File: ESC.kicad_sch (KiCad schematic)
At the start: 37 parts, among them Q1 SP40N03GNJ, Q11 SP40N03GNJ, Q3 SP40N03GNJ, Q5 SP40N03GNJ, Q7 SP40N03GNJ, Q9 SP40N03GNJ, U1 AT32F421G8U7, U3 NSG2065Q_C53463328

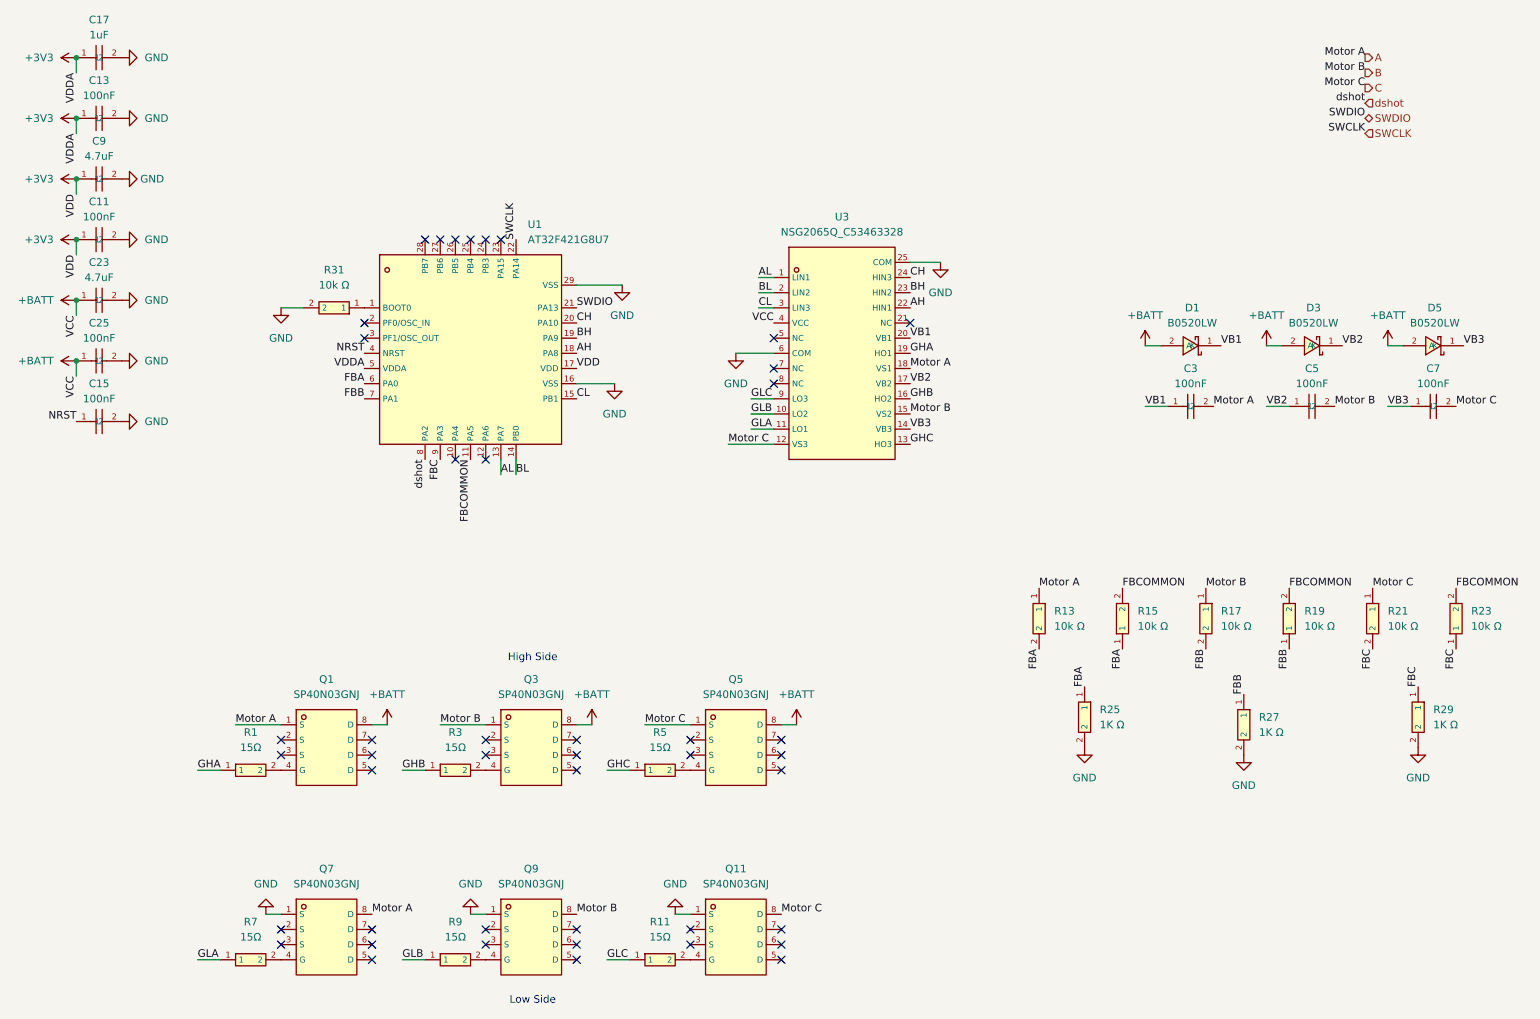
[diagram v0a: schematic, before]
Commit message: Bridges Placed
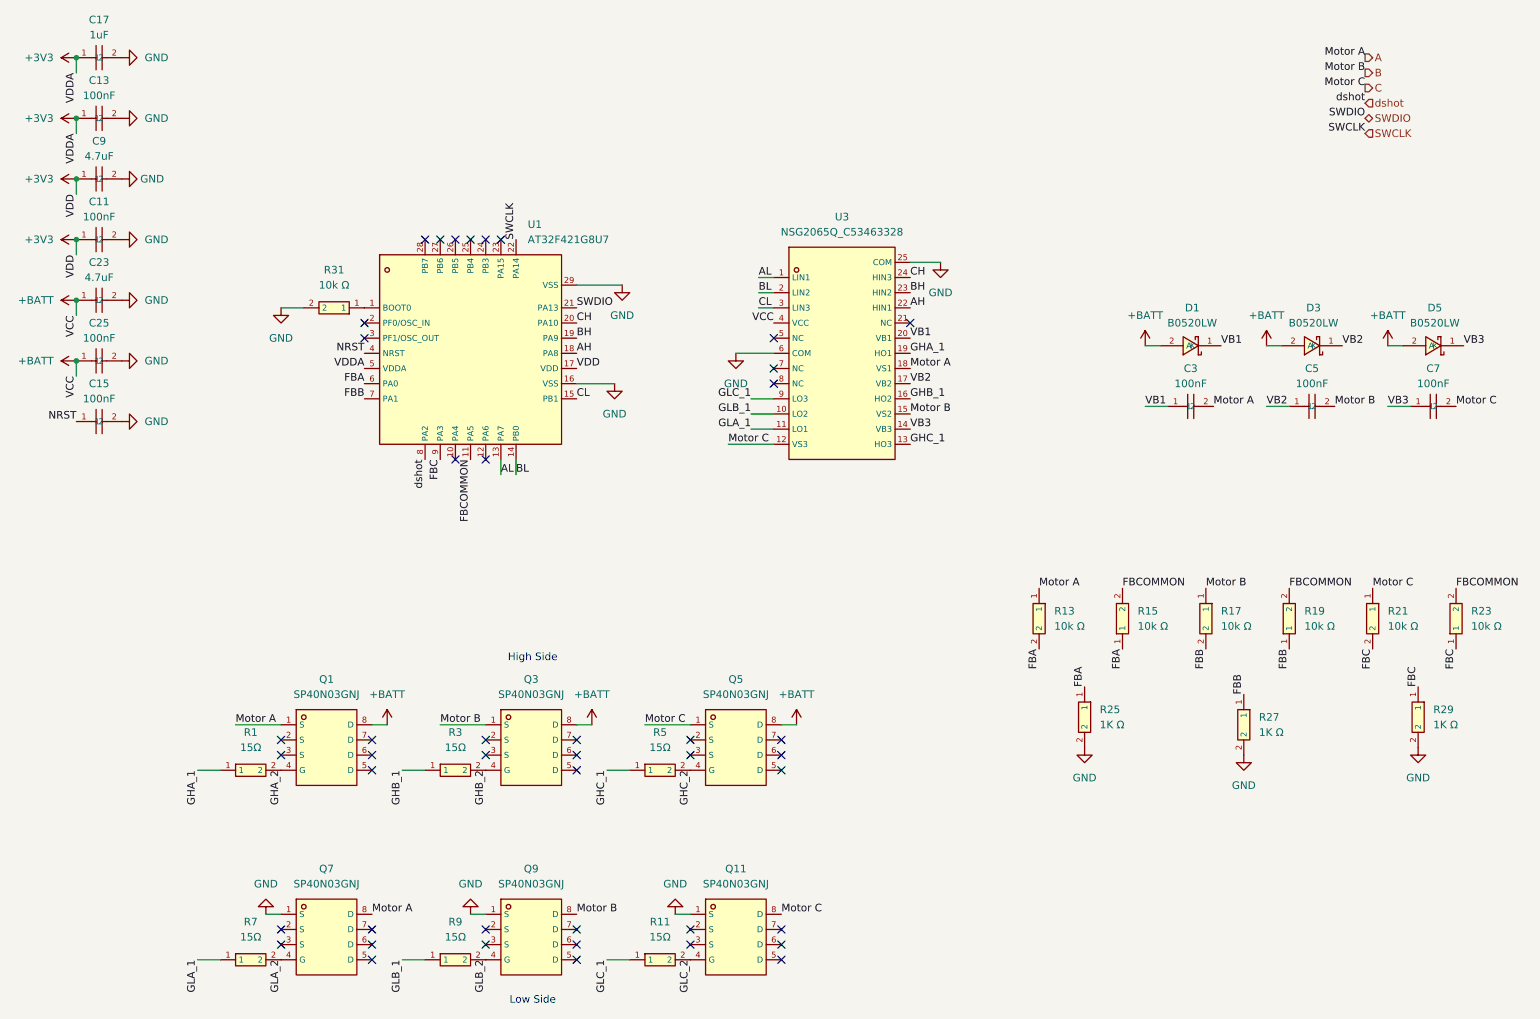
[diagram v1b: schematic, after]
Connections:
- net GHB_2: now reaches Q3.4 (G), R3.2
- net GHA_2: now reaches Q1.4 (G), R1.2
- net GLA_2: now reaches Q7.4 (G), R7.2
- net GLC_2: now reaches Q11.4 (G), R11.2
- net GLB_2: now reaches Q9.4 (G), R9.2
- net GHC_2: now reaches Q5.4 (G), R5.2
- net GHA renamed GHA_1
- net GHB renamed GHB_1
- net GHC renamed GHC_1
- net GLA renamed GLA_1
- net GLB renamed GLB_1
- net GLC renamed GLC_1
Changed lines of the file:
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@@
 		)
 	)
-	(label "GHA"
+	(label "GHA_1"
 		(at 165.1 72.39 0)
 		(effects
@@
 		)
 	)
-	(label "GLB"
-		(at 80.01 173.99 0)
+	(label "GLB_1"
+		(at 80.01 173.99 270)
 		(effects
 			(font
 				(size 1.27 1.27)
 			)
-			(justify left bottom)
+			(justify right bottom)
 		)
 	)
-	(label "GLC"
-		(at 114.3 173.99 0)
+	(label "GLC_1"
+		(at 114.3 173.99 270)
 		(effects
 			(font
 				(size 1.27 1.27)
 			)
-			(justify left bottom)
+			(justify right bottom)
 		)
 	)
@@
 		)
 	)
+	(label "GHC_2"
+		(at 128.27 142.24 270)
+		(effects
+			(font
+				(size 1.27 1.27)
+			)
+			(justify right bottom)
+		)
+	)
 	(label "FBA"
 		(at 194.31 128.27 90)
@@
 		)
 	)
+	(label "GLA_2"
+		(at 59.69 173.99 270)
+		(effects
+			(font
+				(size 1.27 1.27)
+			)
+			(justify right bottom)
+		)
+	)
 	(label "AH"
 		(at 165.1 64.77 0)
@@
 		)
 	)
-	(label "GHC"
-		(at 114.3 142.24 0)
+	(label "GHC_1"
+		(at 114.3 142.24 270)
 		(effects
 			(font
 				(size 1.27 1.27)
 			)
-			(justify left bottom)
+			(justify right bottom)
 		)
 	)
@@
 		)
 	)
-	(label "GLC"
-		(at 138.43 80.01 0)
+	(label "GLC_1"
+		(at 138.43 80.01 180)
 		(effects
 			(font
 				(size 1.27 1.27)
 			)
-			(justify left bottom)
+			(justify right bottom)
 		)
 	)
@@
 		)
 	)
+	(label "GHA_2"
+		(at 59.69 142.24 270)
+		(effects
+			(font
+				(size 1.27 1.27)
+			)
+			(justify right bottom)
+		)
+	)
 	(label "AL"
 		(at 139.7 59.69 0)
@@
 		)
 	)
+	(label "GLC_2"
+		(at 128.27 173.99 270)
+		(effects
+			(font
+				(size 1.27 1.27)
+			)
+			(justify right bottom)
+		)
+	)
 	(label "VB2"
 		(at 237.49 71.12 0)
@@
 		)
 	)
-	(label "GLA"
-		(at 138.43 85.09 0)
+	(label "GLA_1"
+		(at 138.43 85.09 180)
 		(effects
 			(font
 				(size 1.27 1.27)
 			)
-			(justify left bottom)
+			(justify right bottom)
 		)
 	)
@@
 		)
 	)
-	(label "GHA"
-		(at 45.72 142.24 0)
+	(label "GHA_1"
+		(at 45.72 142.24 270)
 		(effects
 			(font
 				(size 1.27 1.27)
 			)
-			(justify left bottom)
+			(justify right bottom)
 		)
 	)
@@
 		)
 	)
-	(label "GLB"
-		(at 138.43 82.55 0)
+	(label "GLB_1"
+		(at 138.43 82.55 180)
 		(effects
 			(font
 				(size 1.27 1.27)
 			)
-			(justify left bottom)
+			(justify right bottom)
 		)
 	)
-	(label "GHB"
-		(at 80.01 142.24 0)
+	(label "GHB_1"
+		(at 80.01 142.24 270)
 		(effects
 			(font
 				(size 1.27 1.27)
 			)
-			(justify left bottom)
+			(justify right bottom)
 		)
 	)
@@
 		)
 	)
+	(label "GHB_2"
+		(at 93.98 142.24 270)
+		(effects
+			(font
+				(size 1.27 1.27)
+			)
+			(justify right bottom)
+		)
+	)
 	(label "BL"
 		(at 99.06 92.71 0)
@@
 		)
 	)
-	(label "GHC"
+	(label "GHC_1"
 		(at 165.1 87.63 0)
 		(effects
@@
 		)
 	)
-	(label "GLA"
-		(at 45.72 173.99 0)
+	(label "GLA_1"
+		(at 45.72 173.99 270)
 		(effects
 			(font
 				(size 1.27 1.27)
 			)
-			(justify left bottom)
+			(justify right bottom)
 		)
 	)
@@
 		)
 	)
+	(label "GLB_2"
+		(at 93.98 173.99 270)
+		(effects
+			(font
+				(size 1.27 1.27)
+			)
+			(justify right bottom)
+		)
+	)
 	(label "FBC"
 		(at 86.36 90.17 270)
@@
 		)
 	)
-	(label "GHB"
+	(label "GHB_1"
 		(at 165.1 80.01 0)
 		(effects
@@
 			"1c14776d-54fa-4aa4-84ff-83fcf02ac64e" "210c4b2c-b7b5-4afb-bbe1-82244aa57942"
 			"27cea6e2-2570-4949-9870-0f26b9f5d113" "3268536a-697a-4589-8e00-d5d9a1d8763a"
-			"38457fb1-0ff9-4de8-a083-952f6d379ee4" "3d57b5e3-a519-4e89-bfc9-aca66393932d"
-			"3d642506-5e34-4f78-abf9-6bbe0df9d44a" "4287f616-c60c-4161-8ffe-5b3adaefae62"
-			"42a3c5e0-11d9-48bc-ab2c-355af146de52" "44f587eb-cdb4-48d7-8a8e-5d6540035753"
-			"476601b6-6a31-41f0-bb64-556e45b247a2" "47b402bb-c529-445d-9f8b-2fe4d615a12a"
+			"36954112-27b1-4dd2-97e6-75232cb6b7e2" "38457fb1-0ff9-4de8-a083-952f6d379ee4"
+			"3d57b5e3-a519-4e89-bfc9-aca66393932d" "3d642506-5e34-4f78-abf9-6bbe0df9d44a"
+			"4287f616-c60c-4161-8ffe-5b3adaefae62" "42a3c5e0-11d9-48bc-ab2c-355af146de52"
+			"44f587eb-cdb4-48d7-8a8e-5d6540035753" "476601b6-6a31-41f0-bb64-556e45b247a2"
+			"47b402bb-c529-445d-9f8b-2fe4d615a12a" "47e6e984-ce4d-46e0-a894-d0e553476655"
 			"487a5da5-8c73-44b8-8f45-696f75e84cf9" "49b0d9c5-4ac3-46b4-bb94-38195561a559"
 			"5554c18c-10f2-4202-acad-f666eb1a5199" "5f31c9c9-b1e9-4680-84a3-119836e01bfc"
@@
 			"72e5c91c-10db-4c17-9aef-84775fb6c08d" "7a246360-7290-4fe9-9eb2-15f22cad05be"
 			"7ae9f1e9-7f2b-4db9-945a-7c243a2aac7c" "7d352e53-bc24-4e10-abfd-73a72e83d091"
-			"803940c6-fc74-4f94-9463-5c23e8082b2a" "80f2d08f-06d7-4e3d-bd34-e546499f1dcb"
-			"82ffd04d-b5d0-40b6-9acd-fe4808f3e225" "906044e8-c01b-45c3-844a-a2f38e330789"
-			"945f3a50-4e10-4ec5-8775-af5ddea6a727" "9500aeae-4a64-4b7a-86a5-6e5b1bf2d8bc"
-			"99e4186a-ded1-4604-b321-c1003a2baaac" "a158936a-291b-4b25-a165-72cfeba2b03c"
-			"a591c4a8-e155-435d-9658-801c9c3ff225" "a691ff35-da9b-4e22-aadf-609c77c3c681"
-			"ab840be0-ba91-430c-b9b2-94033cfbcc96" "b4d92cda-68fc-45f7-9d44-45b7c9baf693"
-			"c05e6ac1-b7e8-4a35-b556-e9009fd8f97d" "c57e1221-b862-4a6b-8167-c85fcd5474f8"
-			"c81988a6-7ba5-4278-bd84-27276524d889" "c84fc5c8-be61-4489-a190-1e0c579690de"
-			"ccb08951-9161-4b2f-94ab-ecc8dbba297b" "cd11e566-cc81-4209-b1b9-2a994aa52d3f"
-			"cfe3d2f2-e0f5-4a7c-b663-e789cfccc89d" "d53a0392-01c4-419e-8e4b-56e4f6060e45"
+			"7f96b949-5d7d-4ae4-9708-a84871d500f6" "803940c6-fc74-4f94-9463-5c23e8082b2a"
+			"80f2d08f-06d7-4e3d-bd34-e546499f1dcb" "82ffd04d-b5d0-40b6-9acd-fe4808f3e225"
+			"906044e8-c01b-45c3-844a-a2f38e330789" "945f3a50-4e10-4ec5-8775-af5ddea6a727"
+			"9500aeae-4a64-4b7a-86a5-6e5b1bf2d8bc" "99e4186a-ded1-4604-b321-c1003a2baaac"
+			"a158936a-291b-4b25-a165-72cfeba2b03c" "a591c4a8-e155-435d-9658-801c9c3ff225"
+			"a691ff35-da9b-4e22-aadf-609c77c3c681" "ab840be0-ba91-430c-b9b2-94033cfbcc96"
+			"b4d92cda-68fc-45f7-9d44-45b7c9baf693" "c05e6ac1-b7e8-4a35-b556-e9009fd8f97d"
+			"c57e1221-b862-4a6b-8167-c85fcd5474f8" "c81988a6-7ba5-4278-bd84-27276524d889"
+			"c84fc5c8-be61-4489-a190-1e0c579690de" "ccb08951-9161-4b2f-94ab-ecc8dbba297b"
+			"cd11e566-cc81-4209-b1b9-2a994aa52d3f" "cfe3d2f2-e0f5-4a7c-b663-e789cfccc89d"
+			"d11460aa-a565-4fc5-99cb-b484b69dd28d" "d53a0392-01c4-419e-8e4b-56e4f6060e45"
 			"d8f45f1b-47a3-46df-9987-5ff606e07901" "d9dc6a10-56b3-4128-b9e0-2af0c56b0640"
-			"e3952114-df84-44be-9d15-8868ad73b842"
+			"e3952114-df84-44be-9d15-8868ad73b842" "fa05d54d-fe14-4402-a9da-3154b8377b48"
 		)
 	)
